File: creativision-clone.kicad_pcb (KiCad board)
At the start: 2 copper layers, 208.8 x 99.7 mm, 106 parts, among them J1 Conn_01x10_Socket, J2 Conn_01x10_Socket, J3 Conn_01x07_Pin, J4 Conn_01x04_Socket, J5 RCJ-013, J6 RCJ-014, P1 Cartridge Slot, Q1 2n4401, SW1 Reset, SW2 Power Toggle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

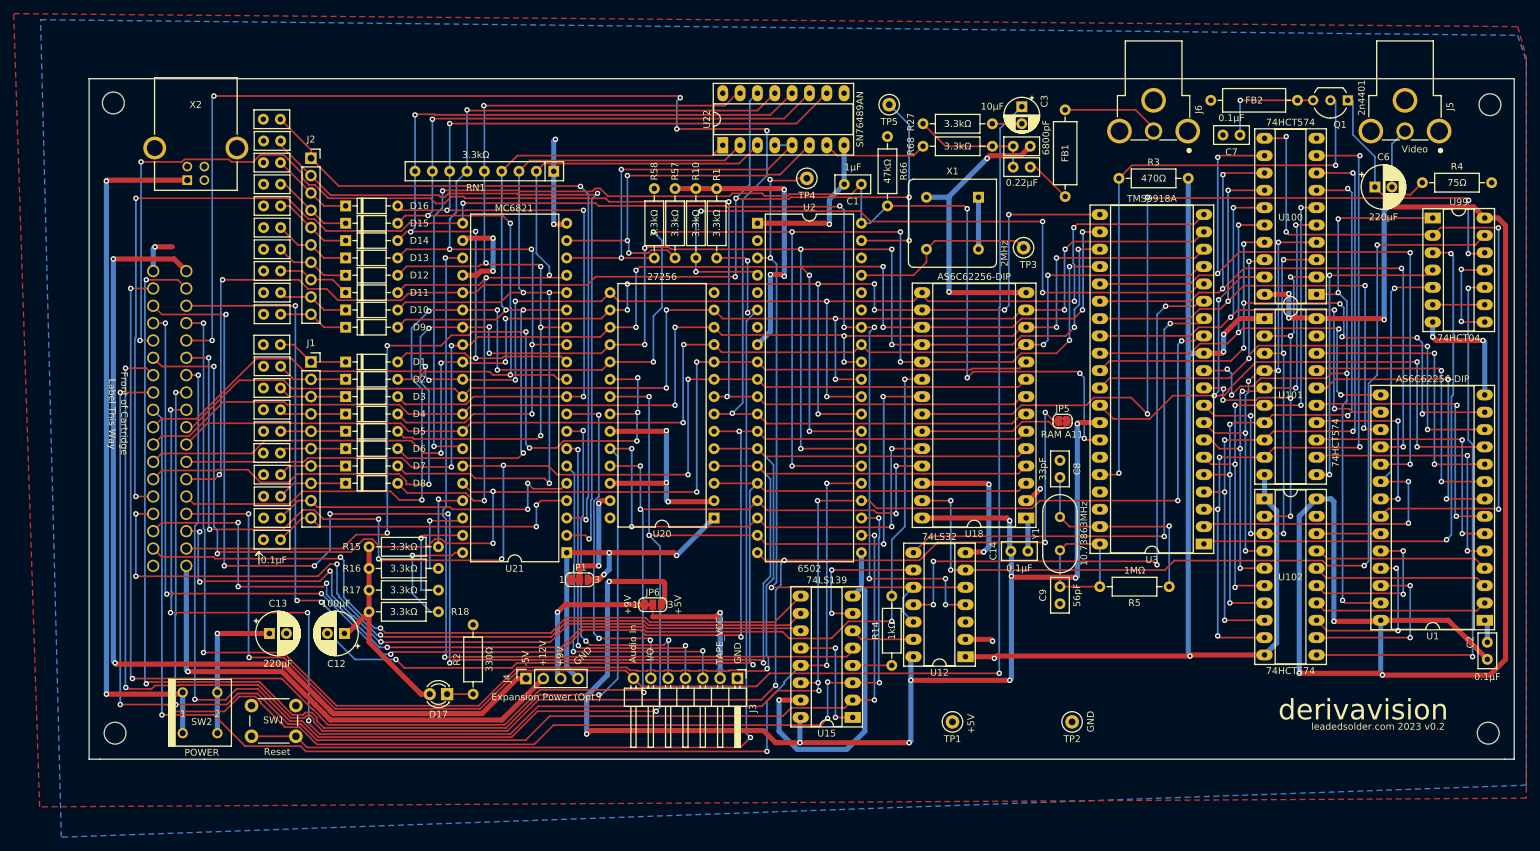
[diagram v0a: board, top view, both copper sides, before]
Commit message: Delete series filter cap (thanks ZephyrZ80)
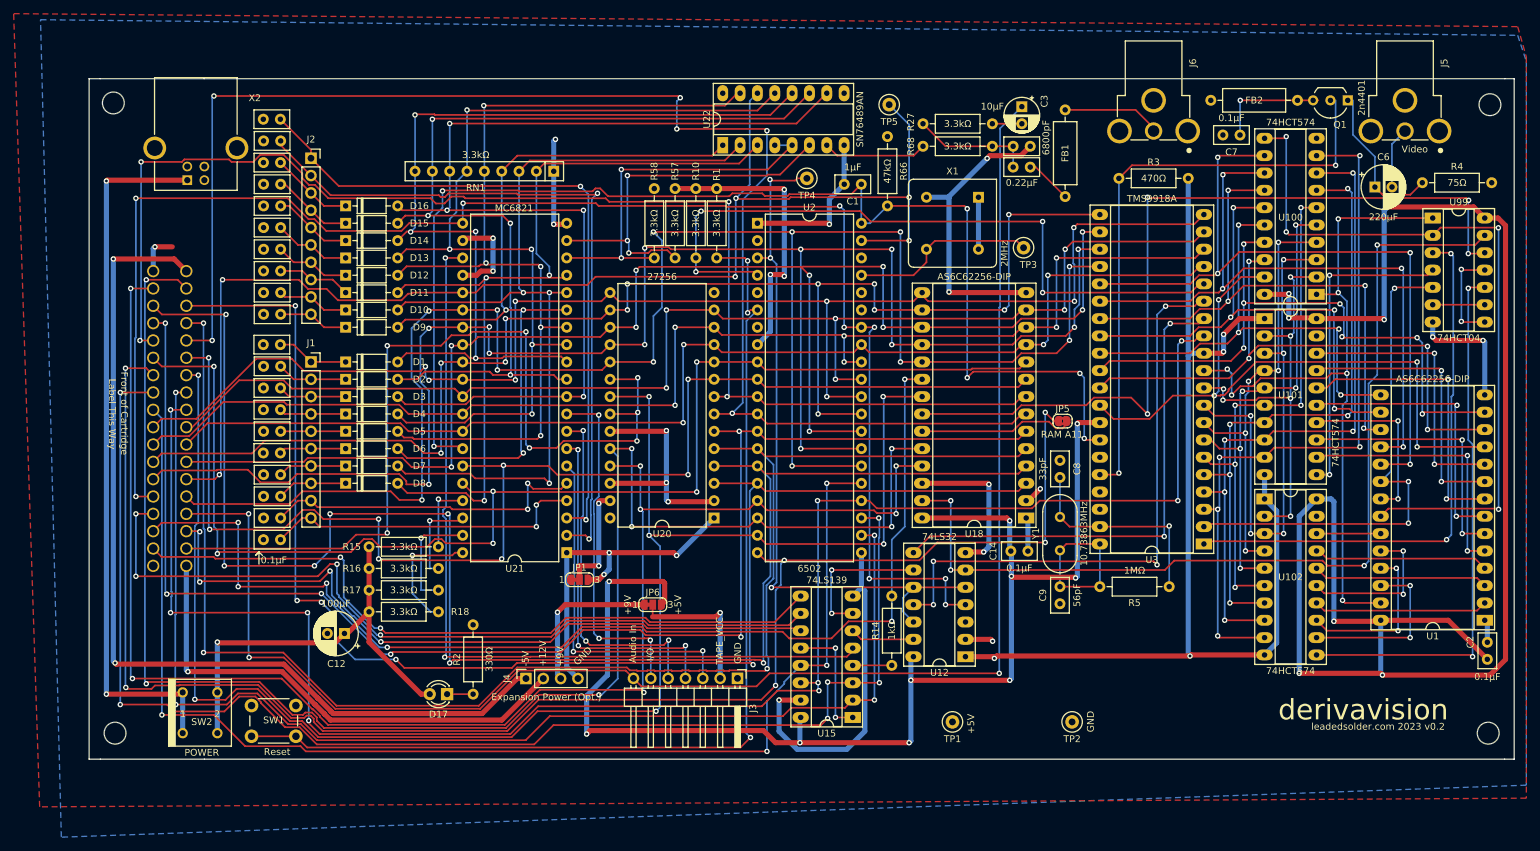
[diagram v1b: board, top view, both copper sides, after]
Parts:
- removed C13: 220µF, Capacitor_THT:CP_Radial_D6.3mm_P2.50mm
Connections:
- SW2 pad 2: /SW_VCC -> +5V
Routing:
- net +5V: track 533.0 -> 565.6 mm, vias 25 -> 26
- net /SW_VCC: track 22.5 -> 0.00 mm, vias 1 -> 0
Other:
- board text added: "En"
- board text added: "Vcc"

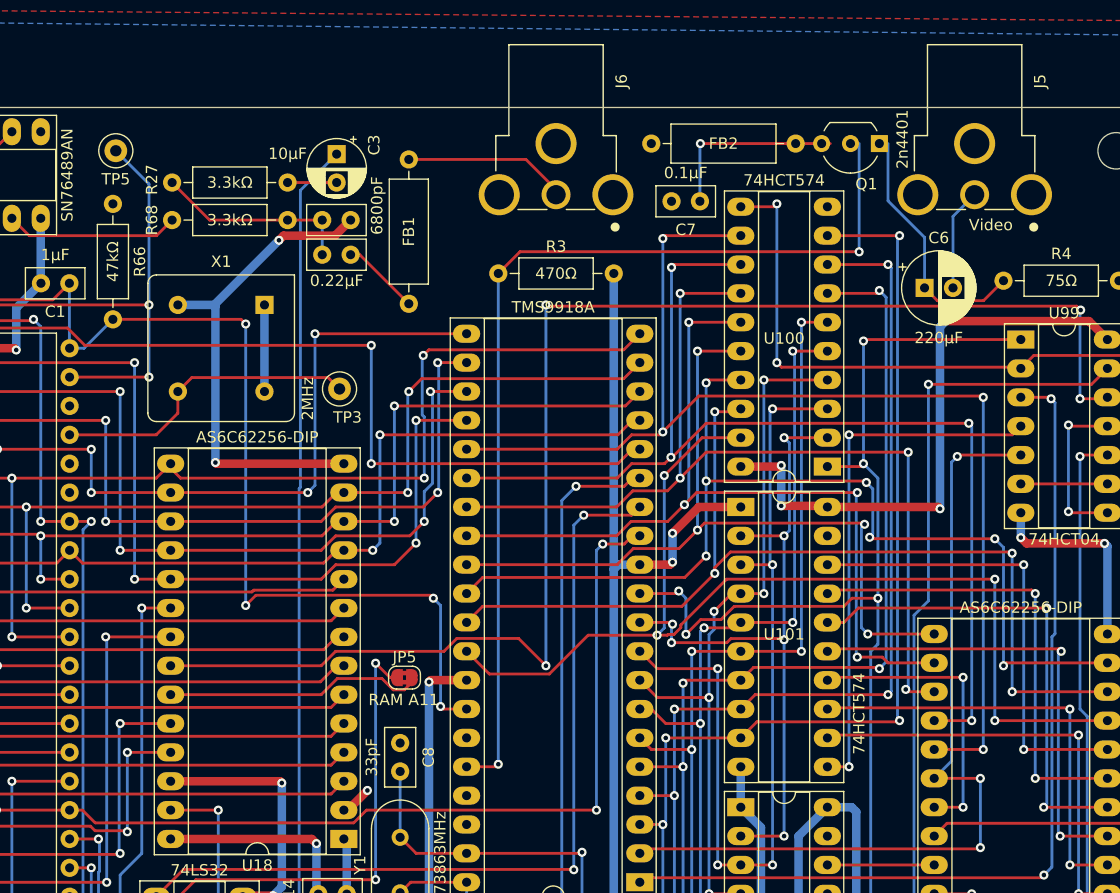
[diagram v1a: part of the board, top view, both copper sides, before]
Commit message: Fix MODE pin on TMS9918
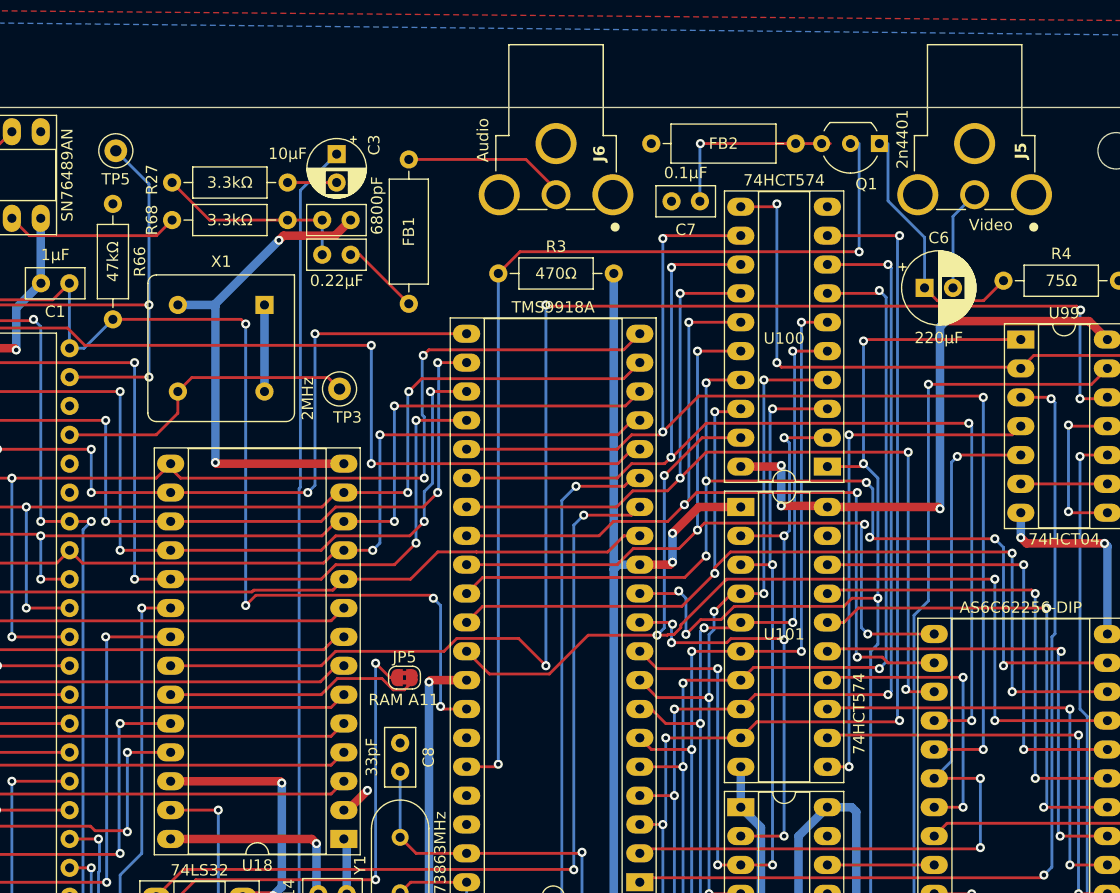
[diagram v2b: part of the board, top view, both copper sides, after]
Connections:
- U3 pad 13: /a14 -> /a0
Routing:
- net /a14: track 258.0 -> 183.5 mm, vias 9 -> 7
- net /a0: track 190.3 -> 217.9 mm
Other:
- board text added: "Audio"
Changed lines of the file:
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@@
     (property "Sheetname" "")
     (attr through_hole)
-    (fp_text reference "U18" (at 7.62 -2.33) (layer "F.SilkS")
+    (fp_text reference "U18" (at 7.62 -2.33 180) (layer "F.SilkS")
         (effects (font (size 1 1) (thickness 0.15)))
     )
-    (fp_text value "AS6C62256-DIP" (at 7.62 35.35) (layer "F.SilkS")
+    (fp_text value "AS6C62256-DIP" (at 7.62 35.35 180) (layer "F.Fab")
         (effects (font (size 1 1) (thickness 0.15)))
     )
-    (fp_text user "${REFERENCE}" (at 7.62 16.51) (layer "F.Fab")
+    (fp_text user "${REFERENCE}" (at 7.62 16.51 180) (layer "F.Fab")
         (effects (font (size 1 1) (thickness 0.15)))
     )
@@
       (net 2 "GND") (pinfunction "GND") (pintype "power_in"))
     (pad "13" thru_hole oval (at 0 30.48 180) (size 2.4 1.6) (drill 0.8) (layers "*.Cu" "*.Mask")
-      (net 110 "/a14") (pinfunction "MODE") (pintype "input"))
+      (net 97 "/a0") (pinfunction "MODE") (pintype "input"))
     (pad "14" thru_hole oval (at 0 33.02 180) (size 2.4 1.6) (drill 0.8) (layers "*.Cu" "*.Mask")
       (net 133 "/~{VDP_CSW}") (pinfunction "~{CSW}") (pintype "input"))
@@
     (property "Sheetname" "")
     (attr through_hole)
-    (fp_text reference "J5" (at -4.030465 -5.762825 -90) (layer "F.SilkS")
-        (effects (font (size 1.001362 1.001362) (thickness 0.015)))
+    (fp_text reference "J5" (at 2.085 -4.064 -90) (layer "F.SilkS")
+        (effects (font (size 1.001362 1.001362) (thickness 0.2) bold))
     )
     (fp_text value "RCJ-013" (at 0.064975 5.495155 -90) (layer "F.Fab")
@@
     (property "Sheetname" "")
     (attr through_hole)
-    (fp_text reference "J6" (at -4.030465 -5.762825 -90) (layer "F.SilkS")
-        (effects (font (size 1.001362 1.001362) (thickness 0.015)))
+    (fp_text reference "J6" (at 2.339 -3.81 -90) (layer "F.SilkS")
+        (effects (font (size 1.001362 1.001362) (thickness 0.2) bold))
     )
     (fp_text value "RCJ-014" (at 0.064975 5.495155 -90) (layer "F.Fab")
@@
     (effects (font (size 1 1) (thickness 0.15)) (justify left bottom))
   )
+  (gr_text "Audio" (at 214.123 48.413929 90) (layer "F.SilkS")
+    (effects (font (size 1 1) (thickness 0.15)) (justify left bottom))
+  )
   (gr_text "+12V" (at 131.065 129.693929 90) (layer "F.SilkS")
     (effects (font (size 1 1) (thickness 0.15)) (justify left bottom))
@@
   (segment (start 249.174 92.456) (end 248.666 91.948) (width 0.25) (layer "F.Cu") (net 82))
   (segment (start 248.666 91.948) (end 246.4695 91.948) (width 0.25) (layer "F.Cu") (net 82))
+  (segment (start 223.750331 81.275) (end 225.015331 80.01) (width 0.25) (layer "F.Cu") (net 82))
+  (segment (start 229.789777 80.01) (end 231.261603 78.538174) (width 0.25) (layer "F.Cu") (net 82))
   (segment (start 246.4695 77.47) (end 232.329777 77.47) (width 0.25) (layer "F.Cu") (net 82))
-  (segment (start 212.095 81.275) (end 225.303 81.275) (width 0.25) (layer "F.Cu") (net 82))
   (segment (start 231.648 62.484) (end 236.22 62.484) (width 0.25) (layer "F.Cu") (net 82))
+  (segment (start 225.015331 80.01) (end 229.789777 80.01) (width 0.25) (layer "F.Cu") (net 82))
   (segment (start 232.329777 77.47) (end 231.261603 78.538174) (width 0.25) (layer "F.Cu") (net 82))
-  (segment (start 225.303 81.275) (end 226.568 80.01) (width 0.25) (layer "F.Cu") (net 82))
-  (segment (start 226.568 80.01) (end 229.789777 80.01) (width 0.25) (layer "F.Cu") (net 82))
+  (segment (start 212.095 81.275) (end 223.750331 81.275) (width 0.25) (layer "F.Cu") (net 82))
   (segment (start 253.238 92.456) (end 249.174 92.456) (width 0.25) (layer "F.Cu") (net 82))
-  (segment (start 229.789777 80.01) (end 231.261603 78.538174) (width 0.25) (layer "F.Cu") (net 82))
   (via (at 246.4695 77.47) (size 0.8) (drill 0.4) (layers "F.Cu" "B.Cu") (net 82))
   (via (at 246.4695 91.948) (size 0.8) (drill 0.4) (layers "F.Cu" "B.Cu") (net 82))
@@
   (segment (start 105.495991 111.042929) (end 104.25 111.042929) (width 0.25) (layer "F.Cu") (net 97))
   (segment (start 118.745 102.87) (end 120.015 104.14) (width 0.25) (layer "F.Cu") (net 97))
+  (segment (start 209.564929 82.69) (end 207.164929 85.09) (width 0.25) (layer "F.Cu") (net 97))
   (segment (start 106.620991 112.167929) (end 105.495991 111.042929) (width 0.25) (layer "F.Cu") (net 97))
   (segment (start 201.295 85.09) (end 200.329501 86.055499) (width 0.25) (layer "F.Cu") (net 97))
   (segment (start 102.363 112.929929) (end 83.059 112.929929) (width 0.25) (layer "F.Cu") (net 97))
+  (segment (start 212.96099 82.69) (end 209.564929 82.69) (width 0.25) (layer "F.Cu") (net 97))
   (segment (start 120.015 104.14) (end 123.090929 104.14) (width 0.25) (layer "F.Cu") (net 97))
   (segment (start 83.059 112.929929) (end 82.805 113.183929) (width 0.25) (layer "F.Cu") (net 97))
@@
   (segment (start 193.37174 86.055499) (end 193.212239 86.215) (width 0.25) (layer "F.Cu") (net 97))
   (segment (start 153.035 85.09) (end 155.575 85.09) (width 0.25) (layer "F.Cu") (net 97))
+  (segment (start 227.335 81.275) (end 225.939396 81.275) (width 0.25) (layer "F.Cu") (net 97))
   (segment (start 74.677 85.751929) (end 73.407 84.481929) (width 0.25) (layer "F.Cu") (net 97))
+  (segment (start 224.510467 82.703929) (end 212.974919 82.703929) (width 0.25) (layer "F.Cu") (net 97))
   (segment (start 123.191 104.039929) (end 123.291071 104.14) (width 0.25) (layer "F.Cu") (net 97))
   (segment (start 123.090929 104.14) (end 123.191 104.039929) (width 0.25) (layer "F.Cu") (net 97))
+  (segment (start 225.939396 81.275) (end 224.510467 82.703929) (width 0.25) (layer "F.Cu") (net 97))
   (segment (start 114.664 111.042929) (end 113.539 112.167929) (width 0.25) (layer "F.Cu") (net 97))
   (segment (start 115.655991 111.042929) (end 114.664 111.042929) (width 0.25) (layer "F.Cu") (net 97))
@@
   (segment (start 163.05 86.215) (end 161.925 85.09) (width 0.25) (layer "F.Cu") (net 97))
   (segment (start 193.212239 86.215) (end 163.05 86.215) (width 0.25) (layer "F.Cu") (net 97))
+  (segment (start 212.974919 82.703929) (end 212.96099 82.69) (width 0.25) (layer "F.Cu") (net 97))
+  (segment (start 207.164929 85.09) (end 201.295 85.09) (width 0.25) (layer "F.Cu") (net 97))
   (segment (start 104.25 111.042929) (end 102.363 112.929929) (width 0.25) (layer "F.Cu") (net 97))
   (segment (start 82.297 85.751929) (end 74.677 85.751929) (width 0.25) (layer "F.Cu") (net 97))
@@
   (segment (start 177.165 105.41) (end 170.7255 105.41) (width 0.25) (layer "F.Cu") (net 110))
   (segment (start 96.192905 137.896024) (end 96.192905 137.642023) (width 0.25) (layer "F.Cu") (net 110))
-  (segment (start 178.29637 105.41) (end 177.165 105.41) (width 0.25) (layer "F.Cu") (net 110))
   (segment (start 129.795 135.535929) (end 125.731 139.599929) (width 0.25) (layer "F.Cu") (net 110))
   (segment (start 96.013 121.819929) (end 75.947 121.819929) (width 0.25) (layer "F.Cu") (net 110))
-  (segment (start 226.685 81.275) (end 225.9605 81.9995) (width 0.25) (layer "F.Cu") (net 110))
-  (segment (start 225.9605 81.9995) (end 224.0705 81.9995) (width 0.25) (layer "F.Cu") (net 110))
-  (segment (start 223.52 105.41) (end 203.28599 105.41) (width 0.25) (layer "F.Cu") (net 110))
   (segment (start 164.847 133.249929) (end 162.561 135.535929) (width 0.25) (layer "F.Cu") (net 110))
   (segment (start 168.265 132.09) (end 170.805 132.09) (width 0.25) (layer "F.Cu") (net 110))
   (segment (start 75.947 92.101929) (end 78.257 92.101929) (width 0.25) (layer "F.Cu") (net 110))
   (segment (start 170.805 132.09) (end 170.815 132.08) (width 0.25) (layer "F.Cu") (net 110))
-  (segment (start 179.42137 106.535) (end 178.29637 105.41) (width 0.25) (layer "F.Cu") (net 110))
-  (segment (start 203.28599 105.41) (end 202.16099 106.535) (width 0.25) (layer "F.Cu") (net 110))
   (segment (start 162.561 135.535929) (end 129.795 135.535929) (width 0.25) (layer "F.Cu") (net 110))
-  (segment (start 202.16099 106.535) (end 179.42137 106.535) (width 0.25) (layer "F.Cu") (net 110))
   (segment (start 97.791706 139.599929) (end 96.140353 137.948576) (width 0.25) (layer "F.Cu") (net 110))
   (segment (start 170.943 133.249929) (end 164.847 133.249929) (width 0.25) (layer "F.Cu") (net 110))
-  (segment (start 227.335 81.275) (end 226.685 81.275) (width 0.25) (layer "F.Cu") (net 110))
   (segment (start 96.140353 137.948576) (end 96.192905 137.896024) (width 0.25) (layer "F.Cu") (net 110))
   (via (at 170.7255 105.41) (size 0.8) (drill 0.4) (layers "F.Cu" "B.Cu") (net 110))
   (via (at 96.192905 137.642023) (size 0.8) (drill 0.4) (layers "F.Cu" "B.Cu") (net 110))
-  (via (at 223.52 105.41) (size 0.8) (drill 0.4) (layers "F.Cu" "B.Cu") (net 110))
-  (via (at 224.0705 81.9995) (size 0.8) (drill 0.4) (layers "F.Cu" "B.Cu") (net 110))
   (via (at 96.013 121.819929) (size 0.8) (drill 0.4) (layers "F.Cu" "B.Cu") (net 110))
   (via (at 170.815 132.08) (size 0.8) (drill 0.4) (layers "F.Cu" "B.Cu") (net 110))
@@
   (segment (start 170.815 105.4995) (end 170.7255 105.41) (width 0.25) (layer "B.Cu") (net 110))
   (segment (start 170.815 132.08) (end 170.815 105.4995) (width 0.25) (layer "B.Cu") (net 110))
-  (segment (start 223.52 105.41) (end 223.52 82.55) (width 0.25) (layer "B.Cu") (net 110))
   (segment (start 76.121309 119.396033) (end 76.121309 118.795837) (width 0.25) (layer "B.Cu") (net 110))
   (segment (start 170.815 132.08) (end 170.815 133.121929) (width 0.25) (layer "B.Cu") (net 110))
   (segment (start 96.192905 137.642023) (end 96.192905 121.999834) (width 0.25) (layer "B.Cu") (net 110))
-  (segment (start 223.52 82.55) (end 224.0705 81.9995) (width 0.25) (layer "B.Cu") (net 110))
   (segment (start 75.947 121.819929) (end 76.049513 121.717416) (width 0.25) (layer "B.Cu") (net 110))
   (segment (start 76.049513 118.724041) (end 76.049513 92.204442) (width 0.25) (layer "B.Cu") (net 110))
